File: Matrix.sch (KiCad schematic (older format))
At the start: 227 parts

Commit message: Update: Work on routing LED connections
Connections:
- wire segments 615 -> 616
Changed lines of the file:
@@
 	3060 1445 3060 1590
 Connection ~ 3060 1590
-Connection ~ 3625 1395
 Wire Wire Line
 	3525 1125 3630 1125
@@
 Connection ~ 3505 2295
 Wire Wire Line
-	3525 1825 3625 1825
-Connection ~ 3625 1825
-Wire Wire Line
 	3975 1825 4080 1825
 Connection ~ 4080 1825
@@
 	8005 2295 8005 2145
 Wire Wire Line
-	1675 1825 1790 1825
-Wire Wire Line
-	1225 2525 1790 2525
+	1790 1825 1675 1825
+Wire Wire Line
+	1790 2525 1225 2525
 Wire Wire Line
 	1575 2625 1655 2625
@@
 Connection ~ 1655 3610
 Wire Wire Line
-	1225 3175 1790 3175
+	1790 3175 1225 3175
 Connection ~ 1575 3275
 Connection ~ 1675 3175
@@
 	3625 4475 3525 4475
 Wire Wire Line
-	3425 4575 3425 3925
+	3425 3925 3425 4575
 Wire Wire Line
 	3425 5095 3425 4570
@@
 Connection ~ 7555 4275
 Wire Wire Line
-	7475 4570 7475 3925
+	7475 3925 7475 4570
 Wire Wire Line
 	7475 5075 7475 4520
@@
 	7925 3925 7925 4625
 Connection ~ 7925 4570
+Wire Wire Line
+	3525 1825 3625 1825
+Connection ~ 3625 1825
+Wire Wire Line
+	3630 1395 3625 1395
 $EndSCHEMATC

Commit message: Update: More routing
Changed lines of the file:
@@
 LIBS:Type-C
 LIBS:dk_Transistors-Bipolar-BJT-Single
+LIBS:dk_Tactile-Switches
 LIBS:co60-cache
 EELAYER 25 0
@@
 	7920 5075 7920 4625
 Wire Wire Line
-	7925 4625 7920 4625
+	7920 4625 7925 4625
 Wire Wire Line
-	7925 3925 7925 4625
+	7925 4625 7925 3925
 Connection ~ 7925 4570
 Wire Wire Line

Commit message: Add: Fields for components that shouldn't be part of the BOM
This ensures that all of the switches won't be added as BOM
lines.
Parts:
- K_#0_1, K_#1, K_#2, K_#3, K_#4, K_#5, K_#6, K_#7, K_#8, K_#9, K_'1, K_,1, K_-1, K_.1, K_/1, K_;1, K_=1, K_A1, K_B1, K_BACK1, K_BACK2, K_C1, K_CAPS1, K_CAPS2, K_D1, K_DEL1, K_E1, K_ENTER1, K_ESC1, K_F1, K_FN1, K_G1, K_H1, K_I1, K_ISO#1, K_ISOENTER1, K_ISO\1, K_J1, K_K1, K_L1, K_LALT1, K_LALT2, K_LCTL1, K_LCTL2, K_LGUI1, K_LGUI2, K_LSHIFT1, K_LSHIFT2, K_M1, K_N1, K_O1, K_P1, K_Q1, K_R1, K_RALT1, K_RALT3, K_RCTL1, K_RCTL2, K_RCTL3, K_RFN1, K_RFN2, K_RFN3, K_RGUI1, K_RMOD1, K_RMOD2, K_RMOD3, K_RSHIFT1, K_RSHIFT2, K_S1, K_SPACE1_1, K_SPACE1_2, K_SPACE1_3, K_SPACE2_1, K_SPACE2_2, K_SPACE2_3, K_SPACE2_4, K_SPACE2_5, K_SPACE3_1, K_SPACE3_2, K_SPACE3_3, K_T1, K_TAB1, K_U1, K_V1, K_W1, K_X1, K_Y1, K_Z1, K_[1, K_\1, K_]1: Config (none) -> dnf

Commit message: Update: Add more info to BOM, and reformat it
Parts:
- D1: Digi-Key_PN (none) -> 1N4148WTPMSCT-ND
- R1: Digi-Key_PN (none) -> MCT0603-560-CFCT-ND
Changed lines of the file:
@@
 F 3 "http://www.mccsemi.com/up_pdf/1N4148W(SOD123).pdf" V 1400 1430 50  0001 C CNN
 F 4 "1N4148W-TP" H 1400 1430 60  0001 C CNN "Product"
+F 5 "1N4148WTPMSCT-ND" H 1400 1430 60  0001 C CNN "Digi-Key_PN"
 	1    1400 1430
 	0    -1   -1   0
@@
 F 3 "https://www.mouser.ca/datasheet/2/427/mcx0x0xpro-223600.pdf" H 1655 1345 50  0001 C CNN
 F 4 "MCT06030C5600FP500" H 1655 1345 60  0001 C CNN "Product"
+F 5 "MCT0603-560-CFCT-ND" H 1655 1345 60  0001 C CNN "Digi-Key_PN"
 	1    1655 1345
 	1    0    0    -1

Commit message: Update: Migrate project to Kicad 5
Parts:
- D1, D10, D11, D12, D13, D14, D15, D16, D17, D18, D19, D2, D20, D21, D22, D23, D24, D25, D26, D27, D28, D29, D3, D30, D31, D32, D33, D34, D35, D36, D37, D38, D39, D4, D40, D41, D42, D43, D44, D45, D46, D47, D48, D49, D5, D50, D51, D52, D53, D54, D55, D56, D57, D58, D59, D6, D60, D61, D62, D63, D64, D65, D66, D67, D68, D7, D8, D9: symbol D_Small -> co60-rescue:D_Small
- K_#0_1, K_#1, K_#2, K_#3, K_#4, K_#5, K_#6, K_#7, K_#8, K_#9, K_'1, K_,1, K_-1, K_.1, K_/1, K_;1, K_=1, K_A1, K_B1, K_BACK2, K_C1, K_D1, K_DEL1, K_E1, K_ESC1, K_F1, K_FN1, K_G1, K_H1, K_I1, K_ISO#1, K_ISO\1, K_J1, K_K1, K_L1, K_LGUI2, K_M1, K_N1, K_O1, K_P1, K_Q1, K_R1, K_RALT3, K_RCTL2, K_RFN2, K_RFN3, K_RGUI1, K_RMOD2, K_S1, K_T1, K_U1, K_V1, K_W1, K_X1, K_Y1, K_Z1, K_[1, K_]1: symbol MX-1U -> MX_Alps_Hybrids:MX-1U
- K_BACK1: symbol MX-2U -> MX_Alps_Hybrids:MX-2U
- K_CAPS1, K_RSHIFT2: symbol MX-1.75U -> MX_Alps_Hybrids:MX-1.75U
- K_CAPS2, K_LALT1, K_LCTL1, K_LGUI1, K_LSHIFT2, K_RALT1, K_RCTL1, K_RFN1, K_RMOD1, K_SPACE2_1, K_SPACE2_5: symbol MX-1.25U -> MX_Alps_Hybrids:MX-1.25U
- K_ENTER1, K_LSHIFT1, K_SPACE1_1, K_SPACE3_2: symbol MX-2.25U -> MX_Alps_Hybrids:MX-2.25U
- K_ISOENTER1: symbol MX-ISO -> MX_Alps_Hybrids:MX-ISO
- K_LALT2, K_LCTL2, K_RCTL3, K_RMOD3, K_SPACE2_4, K_TAB1, K_\1: symbol MX-1.5U -> MX_Alps_Hybrids:MX-1.5U
- K_RSHIFT1, K_SPACE1_2, K_SPACE1_3, K_SPACE3_1, K_SPACE3_3: symbol MX-2.75U -> MX_Alps_Hybrids:MX-2.75U
- K_SPACE2_2: symbol MX-6.25U -> MX_Alps_Hybrids:MX-6.25U
- K_SPACE2_3: symbol MX-7U -> MX_Alps_Hybrids:MX-7U
- R1, R10, R11, R12, R13, R14, R15, R16, R17, R18, R19, R2, R20, R21, R22, R23, R24, R25, R26, R27, R28, R29, R3, R30, R31, R32, R33, R34, R35, R36, R37, R38, R39, R4, R40, R41, R42, R43, R44, R45, R46, R47, R48, R49, R5, R50, R51, R52, R53, R54, R55, R56, R57, R58, R59, R6, R60, R61, R62, R63, R64, R65, R66, R67, R68, R7, R8, R9: symbol R_Small -> co60-rescue:R_Small

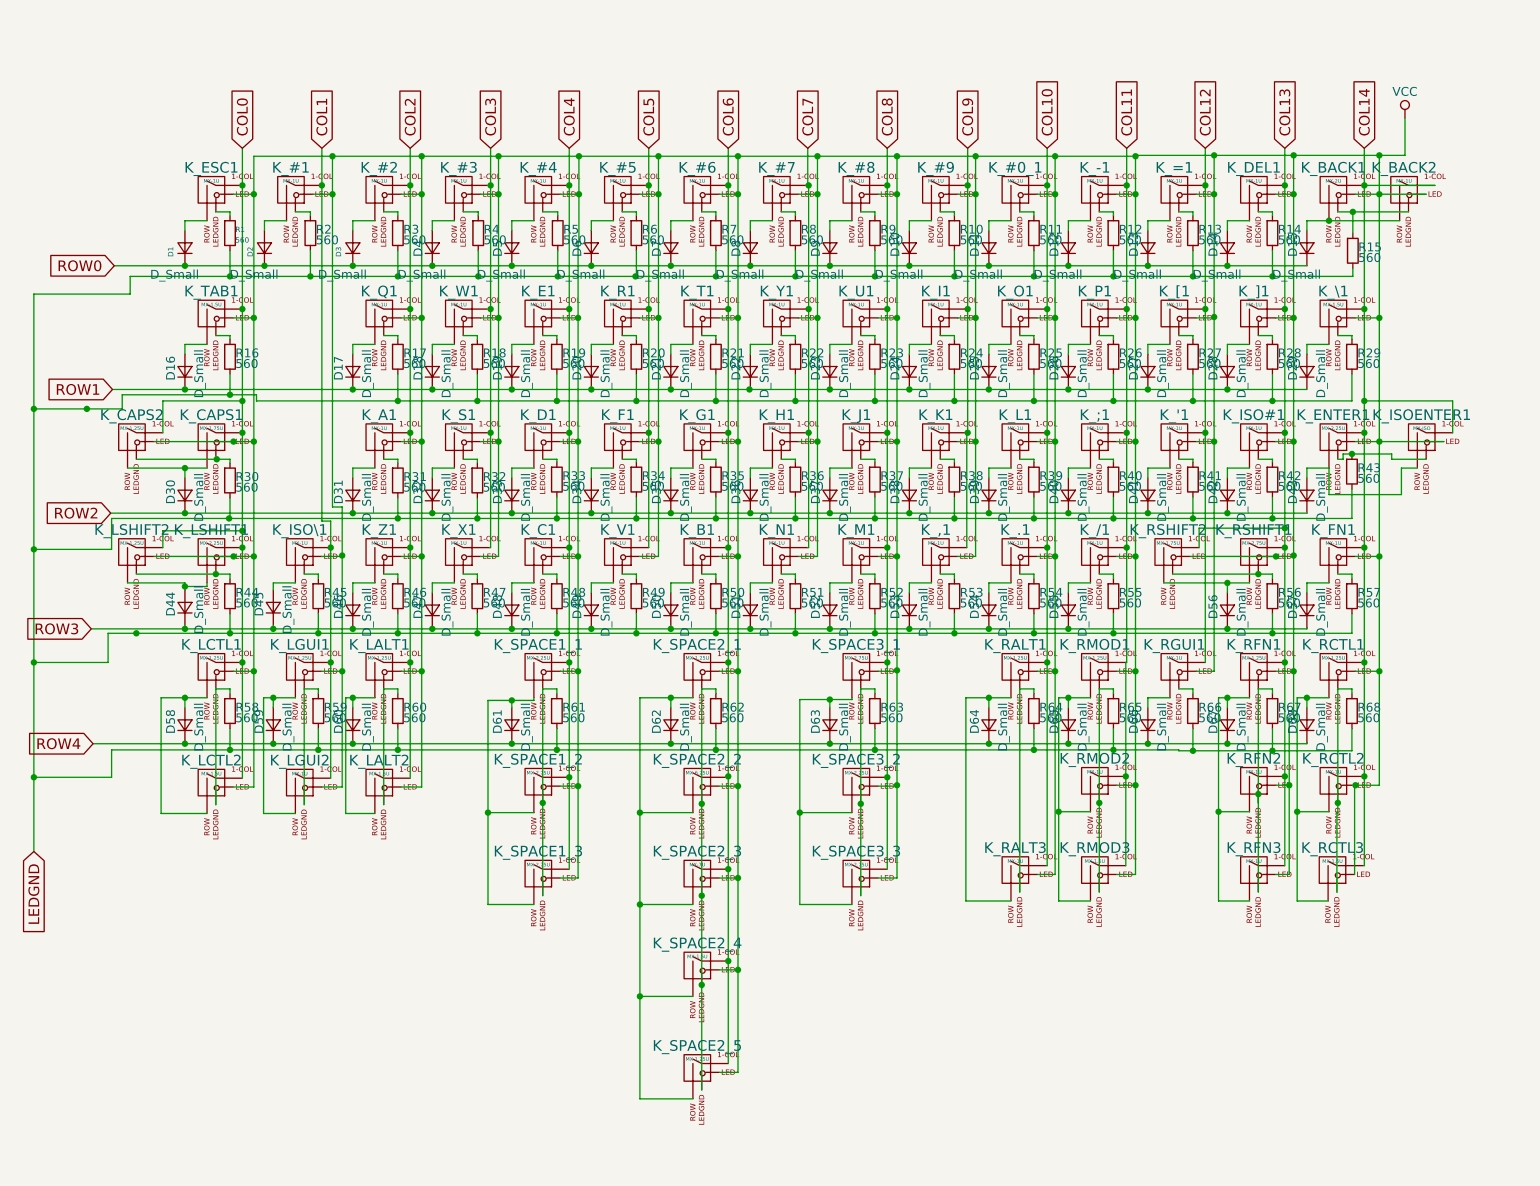
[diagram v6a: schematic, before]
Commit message: Update: Initial work on switching to STM32
The schematic is complete, though may need revising.
The PCB components need to be placed and routed.
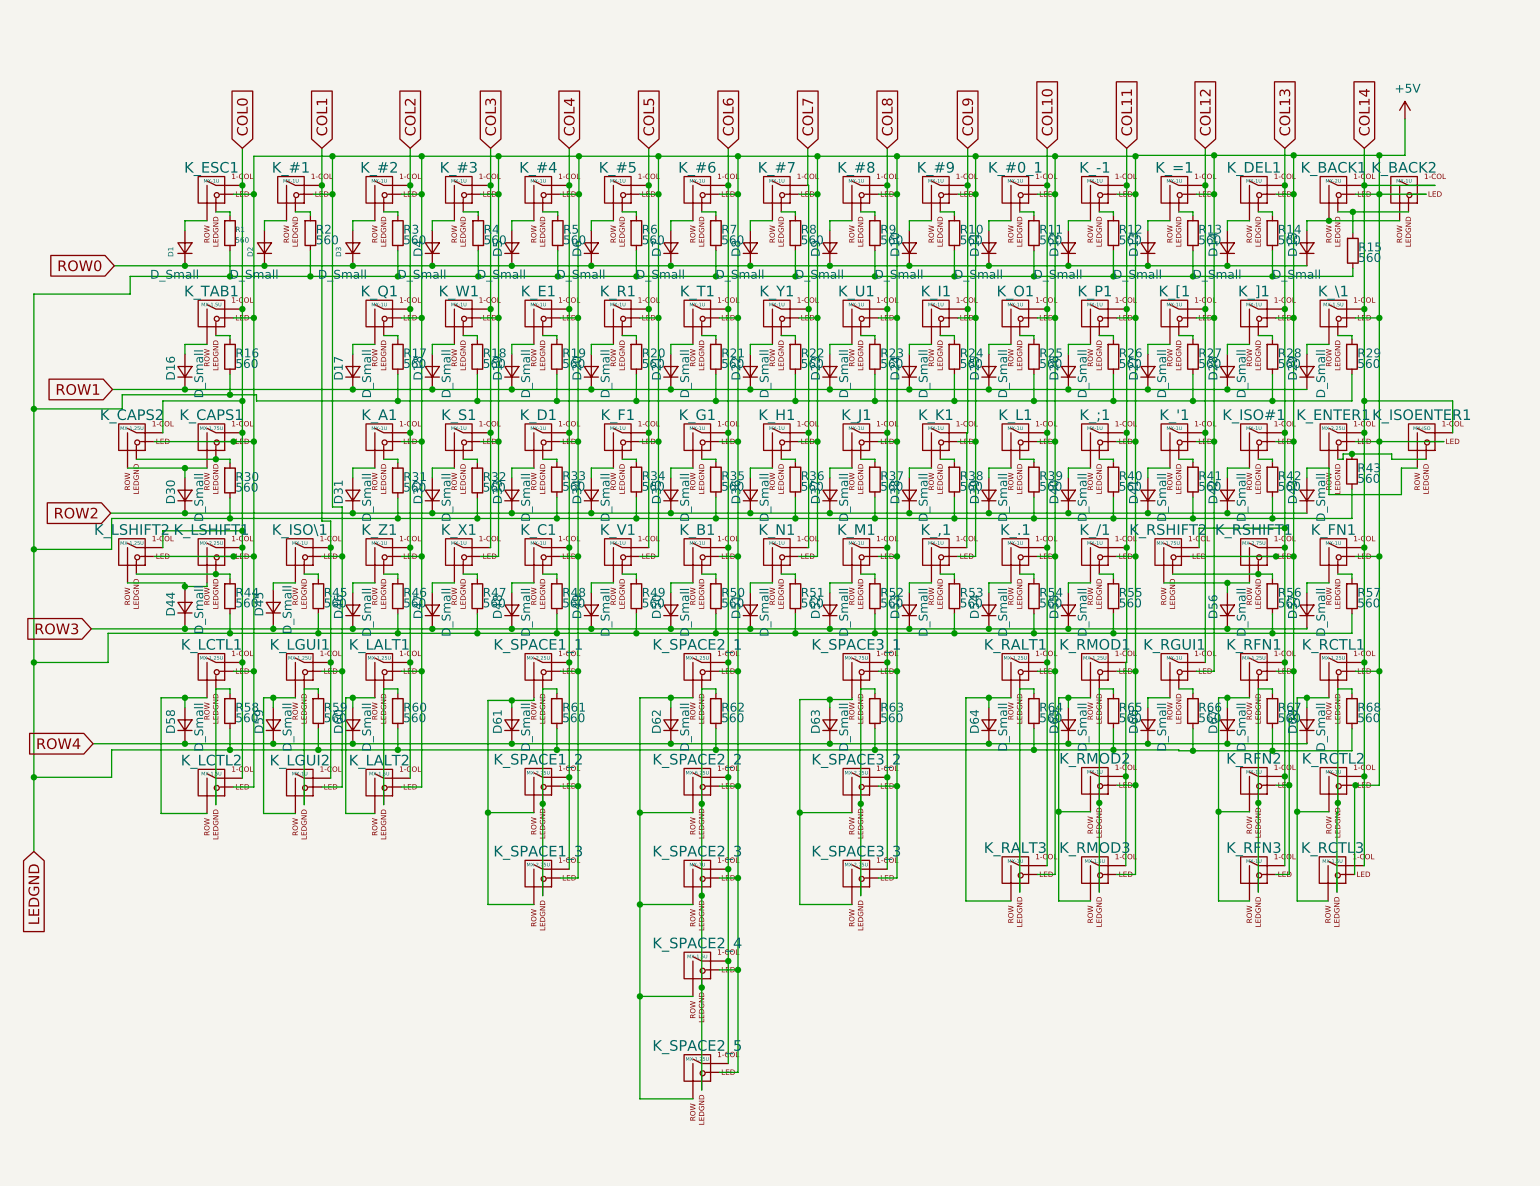
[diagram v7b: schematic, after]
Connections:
- net VCC renamed +5V

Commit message: Update: Clean up routing and work on ground plane
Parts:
- D1: LCSC PN (none) -> C83528
- R1: LCSC PN (none) -> C137619
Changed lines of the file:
@@
 F 4 "1N4148W-TP" H 1400 1430 60  0001 C CNN "Product"
 F 5 "1N4148WTPMSCT-ND" H 1400 1430 60  0001 C CNN "Digi-Key_PN"
+F 6 "C83528" H 1400 1430 50  0001 C CNN "LCSC PN"
 	1    1400 1430
 	0    -1   -1   0
@@
 F 4 "MCT06030C5600FP500" H 1655 1345 60  0001 C CNN "Product"
 F 5 "MCT0603-560-CFCT-ND" H 1655 1345 60  0001 C CNN "Digi-Key_PN"
+F 6 "C137619" H 1655 1345 50  0001 C CNN "LCSC PN"
 	1    1655 1345
 	1    0    0    -1
